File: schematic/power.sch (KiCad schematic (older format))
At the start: 56 parts, among them J6 Conn_01x06, J7 Conn_01x03, U6 BD9E302EFJ, U7 BD9E302EFJ, U8 BD9E302EFJ

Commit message: Changed footprint size of some capacitors
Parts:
- C72, C73, C74, C87, C88, C89, C90, C91, C92: footprint Capacitors_SMD:C_0805 -> Capacitors_SMD:C_1206
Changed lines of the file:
@@
 F 0 "C72" H 6275 2350 50  0000 L CNN
 F 1 "10uF" H 6275 2150 50  0000 L CNN
-F 2 "Capacitors_SMD:C_0805" H 6288 2100 50  0001 C CNN
+F 2 "Capacitors_SMD:C_1206" H 6288 2100 50  0001 C CNN
 F 3 "" H 6250 2250 50  0001 C CNN
 	1    6250 2250
@@
 F 0 "C87" H 8625 2200 50  0000 L CNN
 F 1 "22uF" H 8625 2000 50  0000 L CNN
-F 2 "Capacitors_SMD:C_0805" H 8638 1950 50  0001 C CNN
+F 2 "Capacitors_SMD:C_1206" H 8638 1950 50  0001 C CNN
 F 3 "" H 8600 2100 50  0001 C CNN
 	1    8600 2100
@@
 F 0 "C90" H 8875 2200 50  0000 L CNN
 F 1 "22uF" H 8875 2000 50  0000 L CNN
-F 2 "Capacitors_SMD:C_0805" H 8888 1950 50  0001 C CNN
+F 2 "Capacitors_SMD:C_1206" H 8888 1950 50  0001 C CNN
 F 3 "" H 8850 2100 50  0001 C CNN
 	1    8850 2100
@@
 F 0 "C73" H 6275 4100 50  0000 L CNN
 F 1 "10uF" H 6275 3900 50  0000 L CNN
-F 2 "Capacitors_SMD:C_0805" H 6288 3850 50  0001 C CNN
+F 2 "Capacitors_SMD:C_1206" H 6288 3850 50  0001 C CNN
 F 3 "" H 6250 4000 50  0001 C CNN
 	1    6250 4000
@@
 F 0 "C88" H 8625 3950 50  0000 L CNN
 F 1 "22uF" H 8625 3750 50  0000 L CNN
-F 2 "Capacitors_SMD:C_0805" H 8638 3700 50  0001 C CNN
+F 2 "Capacitors_SMD:C_1206" H 8638 3700 50  0001 C CNN
 F 3 "" H 8600 3850 50  0001 C CNN
 	1    8600 3850
@@
 F 0 "C91" H 8875 3950 50  0000 L CNN
 F 1 "22uF" H 8875 3750 50  0000 L CNN
-F 2 "Capacitors_SMD:C_0805" H 8888 3700 50  0001 C CNN
+F 2 "Capacitors_SMD:C_1206" H 8888 3700 50  0001 C CNN
 F 3 "" H 8850 3850 50  0001 C CNN
 	1    8850 3850
@@
 F 0 "C74" H 6275 5900 50  0000 L CNN
 F 1 "10uF" H 6275 5700 50  0000 L CNN
-F 2 "Capacitors_SMD:C_0805" H 6288 5650 50  0001 C CNN
+F 2 "Capacitors_SMD:C_1206" H 6288 5650 50  0001 C CNN
 F 3 "" H 6250 5800 50  0001 C CNN
 	1    6250 5800
@@
 F 0 "C89" H 8625 5750 50  0000 L CNN
 F 1 "22uF" H 8625 5550 50  0000 L CNN
-F 2 "Capacitors_SMD:C_0805" H 8638 5500 50  0001 C CNN
+F 2 "Capacitors_SMD:C_1206" H 8638 5500 50  0001 C CNN
 F 3 "" H 8600 5650 50  0001 C CNN
 	1    8600 5650
@@
 F 0 "C92" H 8875 5750 50  0000 L CNN
 F 1 "22uF" H 8875 5550 50  0000 L CNN
-F 2 "Capacitors_SMD:C_0805" H 8888 5500 50  0001 C CNN
+F 2 "Capacitors_SMD:C_1206" H 8888 5500 50  0001 C CNN
 F 3 "" H 8850 5650 50  0001 C CNN
 	1    8850 5650

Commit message: Updated inductor footprint
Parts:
- L19, L20: footprint Inductors_SMD_GITHUB:L_Wuerth_HCM-7070 -> Inductors_SMD:L_Taiyo-Yuden_NR-60xx_HandSoldering
- L21: footprint Inductors_SMD_GITHUB:L_Wuerth_HCM-7070 -> Inductors_SMD:L_Taiyo-Yuden_NR-60xx
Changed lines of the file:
@@
 F 0 "L19" V 8100 1950 50  0000 C CNN
 F 1 "4.7uH" V 8225 1950 50  0000 C CNN
-F 2 "Inductors_SMD_GITHUB:L_Wuerth_HCM-7070" H 8150 1950 50  0001 C CNN
+F 2 "Inductors_SMD:L_Taiyo-Yuden_NR-60xx_HandSoldering" H 8150 1950 50  0001 C CNN
 F 3 "" H 8150 1950 50  0001 C CNN
 	1    8150 1950
@@
 F 0 "L20" V 8100 3700 50  0000 C CNN
 F 1 "3.3uH" V 8225 3700 50  0000 C CNN
-F 2 "Inductors_SMD_GITHUB:L_Wuerth_HCM-7070" H 8150 3700 50  0001 C CNN
+F 2 "Inductors_SMD:L_Taiyo-Yuden_NR-60xx_HandSoldering" H 8150 3700 50  0001 C CNN
 F 3 "" H 8150 3700 50  0001 C CNN
 	1    8150 3700
@@
 F 0 "L21" V 8100 5500 50  0000 C CNN
 F 1 "3.3uH" V 8225 5500 50  0000 C CNN
-F 2 "Inductors_SMD_GITHUB:L_Wuerth_HCM-7070" H 8150 5500 50  0001 C CNN
+F 2 "Inductors_SMD:L_Taiyo-Yuden_NR-60xx" H 8150 5500 50  0001 C CNN
 F 3 "" H 8150 5500 50  0001 C CNN
 	1    8150 5500

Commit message: Fixed inductor footprint
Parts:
- L21: footprint Inductors_SMD:L_Taiyo-Yuden_NR-60xx -> Inductors_SMD:L_Taiyo-Yuden_NR-60xx_HandSoldering
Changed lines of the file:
@@
 F 0 "L21" V 8100 5500 50  0000 C CNN
 F 1 "3.3uH" V 8225 5500 50  0000 C CNN
-F 2 "Inductors_SMD:L_Taiyo-Yuden_NR-60xx" H 8150 5500 50  0001 C CNN
+F 2 "Inductors_SMD:L_Taiyo-Yuden_NR-60xx_HandSoldering" H 8150 5500 50  0001 C CNN
 F 3 "" H 8150 5500 50  0001 C CNN
 	1    8150 5500

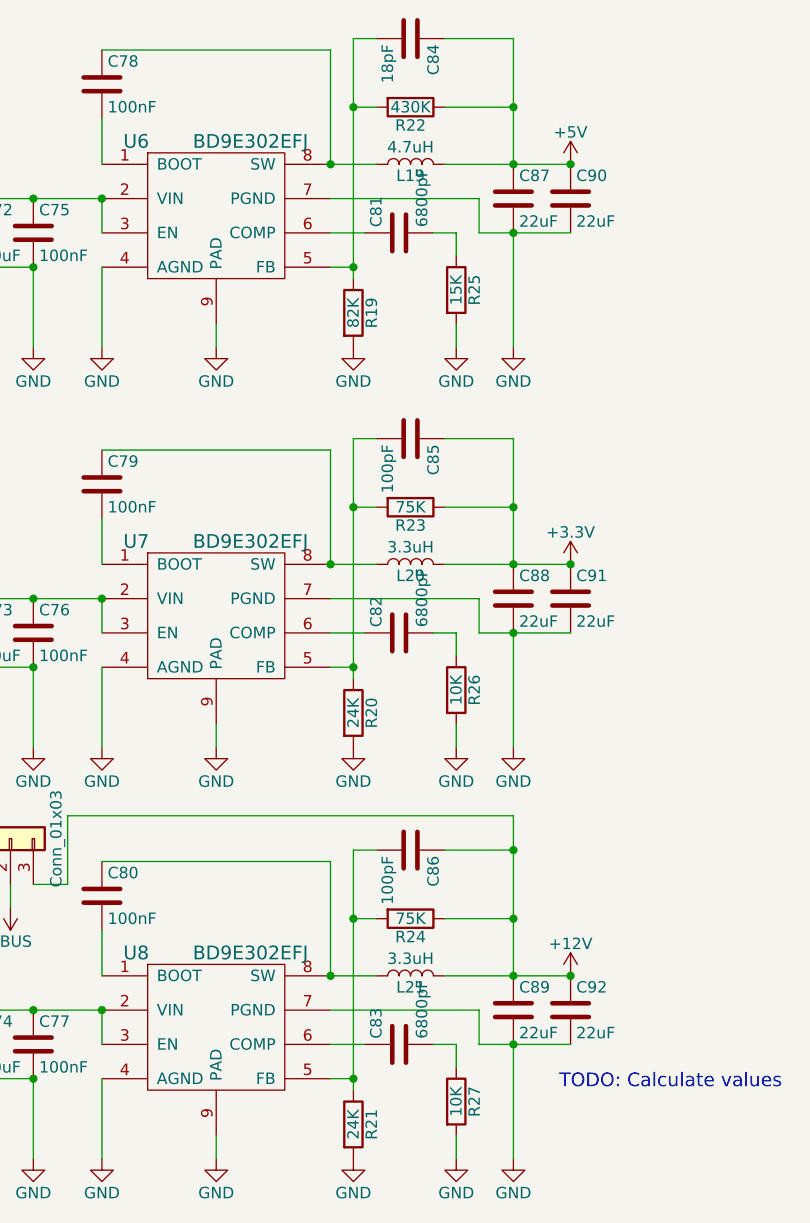
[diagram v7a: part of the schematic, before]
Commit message: Update regulators
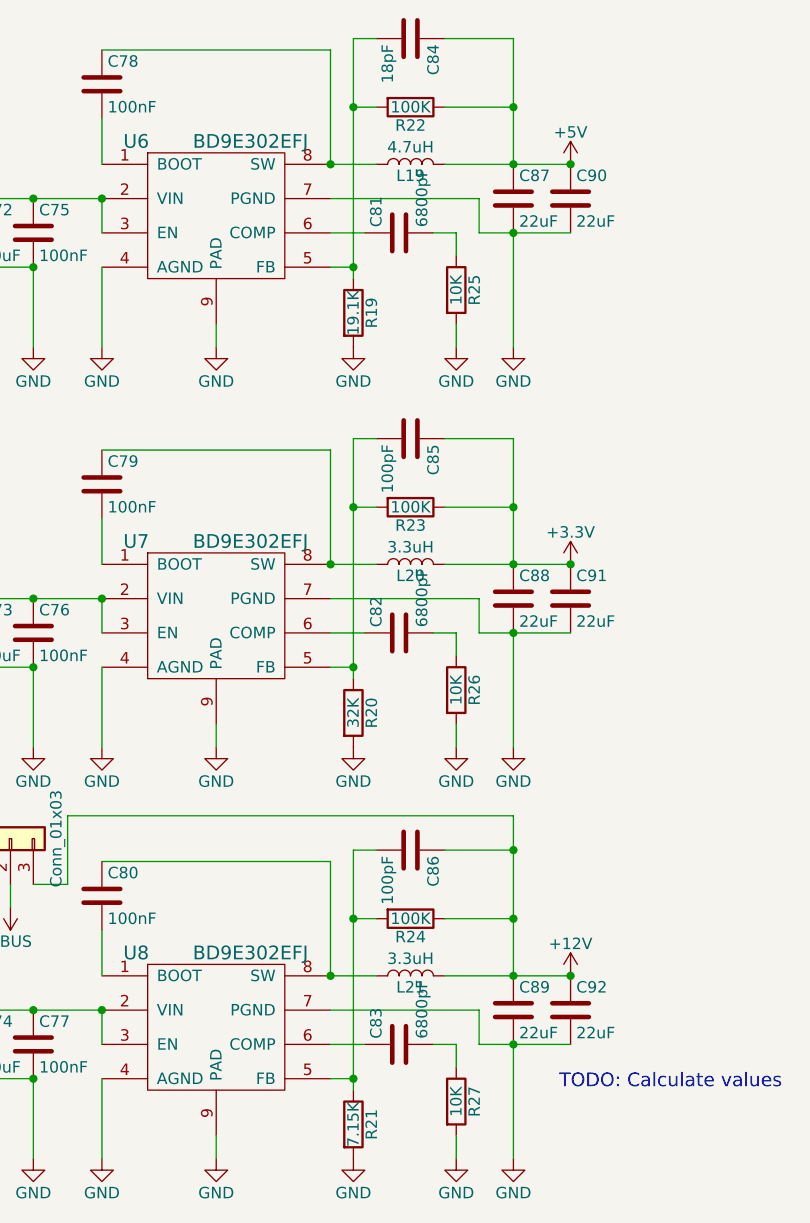
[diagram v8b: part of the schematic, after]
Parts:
- R19: value 82K -> 19.1K
- R20: value 24K -> 32K
- R21: value 24K -> 7.15K
- R22: value 430K -> 100K
- R23, R24: value 75K -> 100K
- R25: value 15K -> 10K
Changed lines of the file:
@@
 P 7900 2600
 F 0 "R19" V 7980 2600 50  0000 C CNN
-F 1 "82K" V 7900 2600 50  0000 C CNN
+F 1 "19.1K" V 7900 2600 50  0000 C CNN
 F 2 "Resistors_SMD:R_0603" V 7830 2600 50  0001 C CNN
 F 3 "" H 7900 2600 50  0001 C CNN
@@
 P 8150 1700
 F 0 "R22" V 8230 1700 50  0000 C CNN
-F 1 "430K" V 8150 1700 50  0000 C CNN
+F 1 "100K" V 8150 1700 50  0000 C CNN
 F 2 "Resistors_SMD:R_0603" V 8080 1700 50  0001 C CNN
 F 3 "" H 8150 1700 50  0001 C CNN
@@
 P 8350 2500
 F 0 "R25" V 8430 2500 50  0000 C CNN
-F 1 "15K" V 8350 2500 50  0000 C CNN
+F 1 "10K" V 8350 2500 50  0000 C CNN
 F 2 "Resistors_SMD:R_0603" V 8280 2500 50  0001 C CNN
 F 3 "" H 8350 2500 50  0001 C CNN
@@
 P 7900 4350
 F 0 "R20" V 7980 4350 50  0000 C CNN
-F 1 "24K" V 7900 4350 50  0000 C CNN
+F 1 "32K" V 7900 4350 50  0000 C CNN
 F 2 "Resistors_SMD:R_0603" V 7830 4350 50  0001 C CNN
 F 3 "" H 7900 4350 50  0001 C CNN
@@
 P 8150 3450
 F 0 "R23" V 8230 3450 50  0000 C CNN
-F 1 "75K" V 8150 3450 50  0000 C CNN
+F 1 "100K" V 8150 3450 50  0000 C CNN
 F 2 "Resistors_SMD:R_0603" V 8080 3450 50  0001 C CNN
 F 3 "" H 8150 3450 50  0001 C CNN
@@
 P 7900 6150
 F 0 "R21" V 7980 6150 50  0000 C CNN
-F 1 "24K" V 7900 6150 50  0000 C CNN
+F 1 "7.15K" V 7900 6150 50  0000 C CNN
 F 2 "Resistors_SMD:R_0603" V 7830 6150 50  0001 C CNN
 F 3 "" H 7900 6150 50  0001 C CNN
@@
 P 8150 5250
 F 0 "R24" V 8230 5250 50  0000 C CNN
-F 1 "75K" V 8150 5250 50  0000 C CNN
+F 1 "100K" V 8150 5250 50  0000 C CNN
 F 2 "Resistors_SMD:R_0603" V 8080 5250 50  0001 C CNN
 F 3 "" H 8150 5250 50  0001 C CNN
